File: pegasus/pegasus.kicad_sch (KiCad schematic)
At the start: 9 parts, among them IC1 Adafruit_MPL3115A2, IC2 Adafruit-BNO055-PCB, IC3 L70B-M39, IC4 RFD900, U1 Teensy4.1

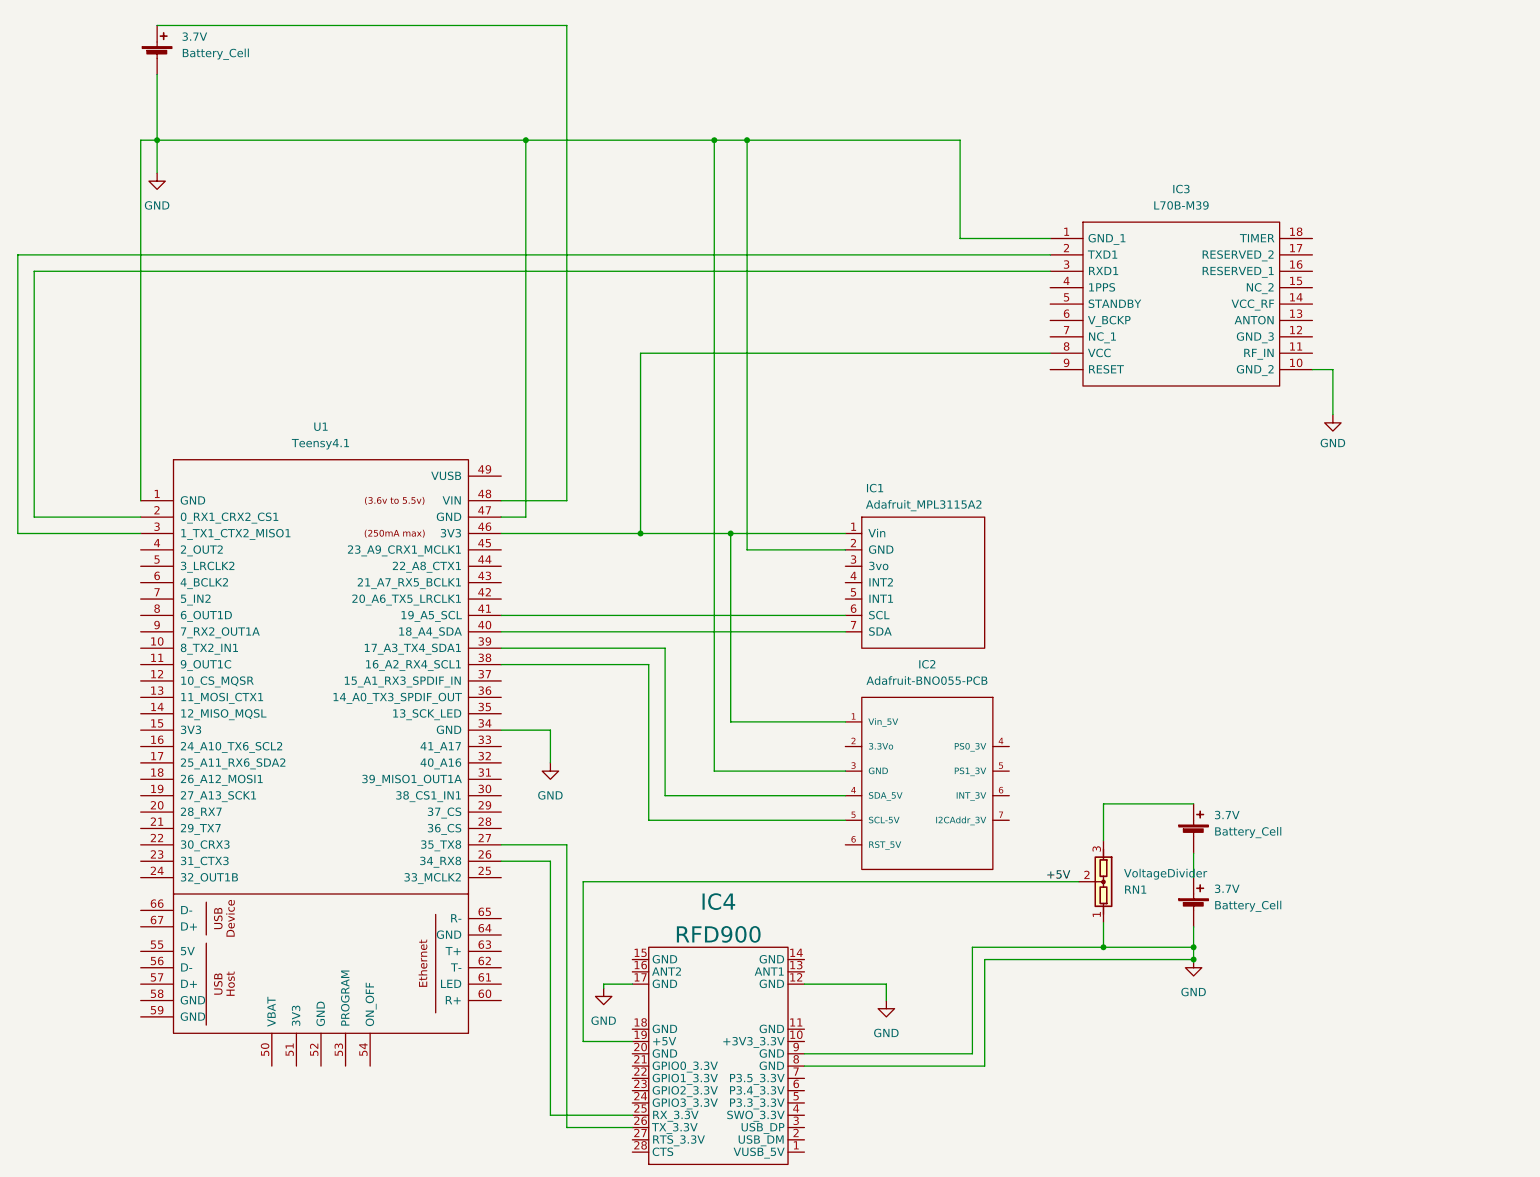
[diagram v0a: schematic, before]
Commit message: Added more components and attached footprints
added voltage regulator for rfd900, battery connectors and updated footprints for all components.
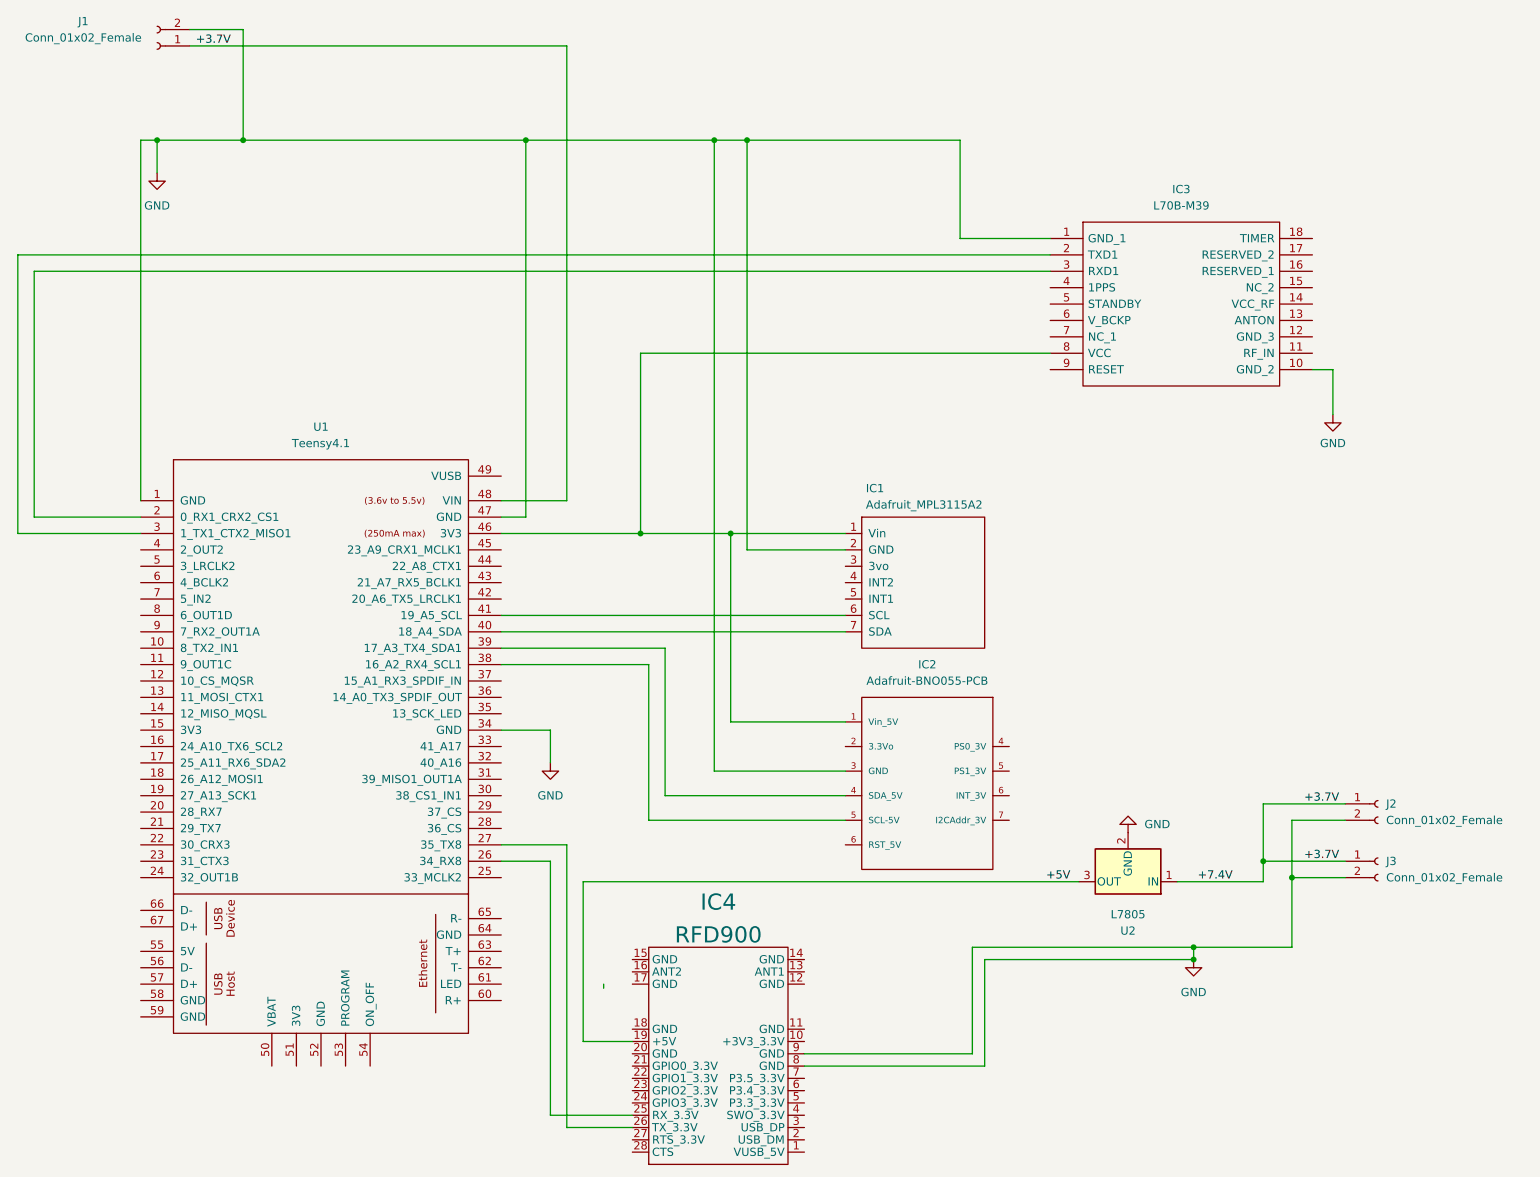
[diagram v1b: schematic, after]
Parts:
- removed 3.7V (x3): Battery_Cell, symbol Device:Battery_Cell
- removed RN1: VoltageDivider, symbol Device:VoltageDivider
- added J1, J2, J3: Conn_01x02_Female, Connector_PinHeader_2.00mm:PinHeader_1x02_P2.00mm_Horizontal, symbol Connector:Conn_01x02_Female
- added U2: L7805, symbol Regulator_Linear:L7805
- IC1: footprint MPL3115A2:1x07 -> Adafruit_MPL3115A2:1x07
- IC2: footprint BNO055:1X10_ROUND_76 -> Adafruit_BNO055:adafruit_
- U1: footprint (none) -> Teensy_4.1:Teensy_4.1
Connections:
- net +5V: now also U2.3 (OUT)
- net GND: now also J1.2 (Pin_2), J2.2 (Pin_2), J3.2 (Pin_2), U2.2 (GND); no longer IC4.12 (GND), IC4.17 (GND)
- net +3.7V: now reaches U1.48 (VIN)
- net +3.7V: now also J1.1 (Pin_1), J2.1 (Pin_1), J3.1 (Pin_1), U2.1 (IN)

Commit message: changed connector footprints from horizontal to vertical
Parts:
- J1, J2, J3: footprint Connector_PinHeader_2.00mm:PinHeader_1x02_P2.00mm_Horizontal -> Connector_PinHeader_2.00mm:PinHeader_1x02_P2.00mm_Vertical
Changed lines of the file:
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@@
       (effects (font (size 1.27 1.27)) (justify left))
     )
-    (property "Footprint" "Connector_PinHeader_2.00mm:PinHeader_1x02_P2.00mm_Horizontal" (id 2) (at 233.68 138.43 0)
+    (property "Footprint" "Connector_PinHeader_2.00mm:PinHeader_1x02_P2.00mm_Vertical" (id 2) (at 233.68 138.43 0)
       (effects (font (size 1.27 1.27)) hide)
     )
@@
       (effects (font (size 1.27 1.27)) (justify left))
     )
-    (property "Footprint" "Connector_PinHeader_2.00mm:PinHeader_1x02_P2.00mm_Horizontal" (id 2) (at 233.68 147.32 0)
+    (property "Footprint" "Connector_PinHeader_2.00mm:PinHeader_1x02_P2.00mm_Vertical" (id 2) (at 233.68 147.32 0)
       (effects (font (size 1.27 1.27)) hide)
     )
@@
     (property "Reference" "J1" (id 0) (at 33.02 17.145 0))
     (property "Value" "Conn_01x02_Female" (id 1) (at 33.02 19.685 0))
-    (property "Footprint" "Connector_PinHeader_2.00mm:PinHeader_1x02_P2.00mm_Horizontal" (id 2) (at 44.45 20.955 0)
+    (property "Footprint" "Connector_PinHeader_2.00mm:PinHeader_1x02_P2.00mm_Vertical" (id 2) (at 44.45 20.955 0)
       (effects (font (size 1.27 1.27)) hide)
     )
@@
     )
     (path "/50f78511-b951-4dcf-a410-ebb84e2ce437"
-      (reference "J1") (unit 1) (value "Conn_01x02_Female") (footprint "Connector_PinHeader_2.00mm:PinHeader_1x02_P2.00mm_Horizontal")
+      (reference "J1") (unit 1) (value "Conn_01x02_Female") (footprint "Connector_PinHeader_2.00mm:PinHeader_1x02_P2.00mm_Vertical")
     )
     (path "/0ea184c9-73d1-4b8a-8896-3886b45cbf01"
-      (reference "J2") (unit 1) (value "Conn_01x02_Female") (footprint "Connector_PinHeader_2.00mm:PinHeader_1x02_P2.00mm_Horizontal")
+      (reference "J2") (unit 1) (value "Conn_01x02_Female") (footprint "Connector_PinHeader_2.00mm:PinHeader_1x02_P2.00mm_Vertical")
     )
     (path "/419715bf-ffaa-4f14-ba39-b7cca3633324"
-      (reference "J3") (unit 1) (value "Conn_01x02_Female") (footprint "Connector_PinHeader_2.00mm:PinHeader_1x02_P2.00mm_Horizontal")
+      (reference "J3") (unit 1) (value "Conn_01x02_Female") (footprint "Connector_PinHeader_2.00mm:PinHeader_1x02_P2.00mm_Vertical")
     )
     (path "/0c9ca546-3290-4390-b47a-32e3591868b6"

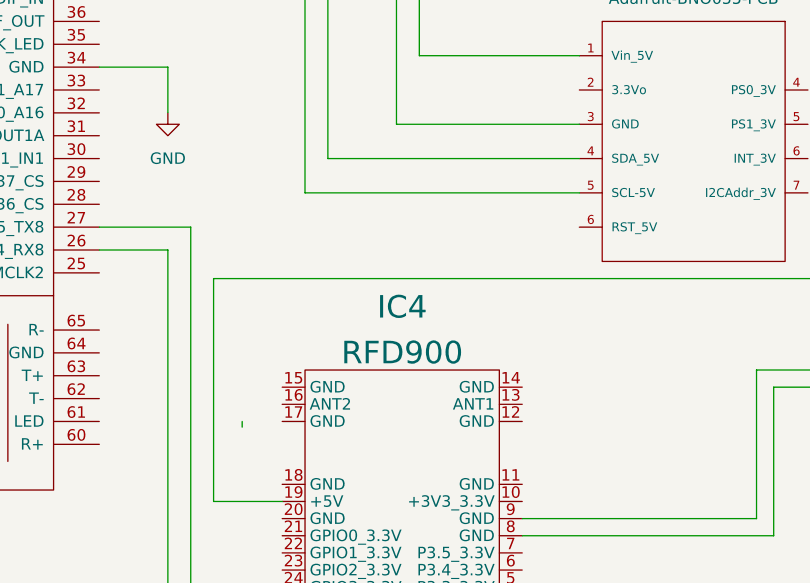
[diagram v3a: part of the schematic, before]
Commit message: adding sma coaxial connectors, footprint may change
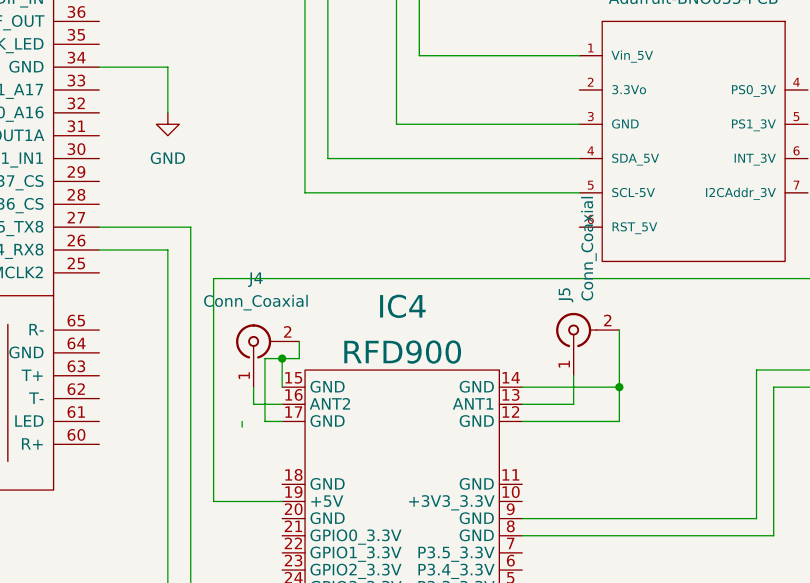
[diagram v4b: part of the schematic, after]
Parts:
- added J4, J5: Conn_Coaxial, Connector_Coaxial:SMA_Molex_73251-1153_EdgeMount_Horizontal, symbol Connector:Conn_Coaxial
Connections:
- net at IC4.12 (GND): now also IC4.14 (GND), J5.2 (Ext)
- net at IC4.13 (ANT1): now also J5.1 (In)
- net at IC4.15 (GND): now also IC4.17 (GND), J4.2 (Ext)
- net at IC4.16 (ANT2): now also J4.1 (In)
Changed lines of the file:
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@@
   (junction (at 135.89 35.56) (diameter 0) (color 0 0 0 0)
   )
+  (junction (at 118.11 159.385) (diameter 0) (color 0 0 0 0)
+  )
+  (junction (at 155.575 162.56) (diameter 0) (color 0 0 0 0)
+  )
   (junction (at 130.81 35.56) (diameter 0) (color 0 0 0 0)
   )
@@
     (stroke (width 0) (type default) (color 0 0 0 0))
   )
+  (wire (pts (xy 144.78 164.465) (xy 150.495 164.465))
+    (stroke (width 0) (type default) (color 0 0 0 0))
+  )
   (wire (pts (xy 220.345 149.86) (xy 228.6 149.86))
     (stroke (width 0) (type default) (color 0 0 0 0))
@@
     (stroke (width 0) (type default) (color 0 0 0 0))
   )
+  (wire (pts (xy 150.495 164.465) (xy 150.495 161.29))
+    (stroke (width 0) (type default) (color 0 0 0 0))
+  )
   (wire (pts (xy 133.35 125.73) (xy 151.13 125.73))
     (stroke (width 0) (type default) (color 0 0 0 0))
@@
     (stroke (width 0) (type default) (color 0 0 0 0))
   )
+  (wire (pts (xy 120.015 157.48) (xy 120.015 159.385))
+    (stroke (width 0) (type default) (color 0 0 0 0))
+  )
+  (wire (pts (xy 118.11 166.37) (xy 116.205 166.37))
+    (stroke (width 0) (type default) (color 0 0 0 0))
+  )
   (wire (pts (xy 144.78 179.07) (xy 172.72 179.07))
     (stroke (width 0) (type default) (color 0 0 0 0))
   )
+  (wire (pts (xy 116.205 159.385) (xy 118.11 159.385))
+    (stroke (width 0) (type default) (color 0 0 0 0))
+  )
   (wire (pts (xy 110.49 175.26) (xy 118.11 175.26))
     (stroke (width 0) (type default) (color 0 0 0 0))
@@
     (stroke (width 0) (type default) (color 0 0 0 0))
   )
+  (wire (pts (xy 144.78 162.56) (xy 155.575 162.56))
+    (stroke (width 0) (type default) (color 0 0 0 0))
+  )
   (wire (pts (xy 25.4 55.88) (xy 182.88 55.88))
     (stroke (width 0) (type default) (color 0 0 0 0))
@@
     (stroke (width 0) (type default) (color 0 0 0 0))
   )
+  (wire (pts (xy 155.575 162.56) (xy 155.575 166.37))
+    (stroke (width 0) (type default) (color 0 0 0 0))
+  )
   (wire (pts (xy 97.79 111.76) (xy 151.13 111.76))
     (stroke (width 0) (type default) (color 0 0 0 0))
@@
     (stroke (width 0) (type default) (color 0 0 0 0))
   )
+  (wire (pts (xy 114.935 162.56) (xy 114.935 164.465))
+    (stroke (width 0) (type default) (color 0 0 0 0))
+  )
   (wire (pts (xy 120.65 140.97) (xy 151.13 140.97))
     (stroke (width 0) (type default) (color 0 0 0 0))
@@
     (stroke (width 0) (type default) (color 0 0 0 0))
   )
+  (wire (pts (xy 118.11 159.385) (xy 118.11 162.56))
+    (stroke (width 0) (type default) (color 0 0 0 0))
+  )
   (wire (pts (xy 49.53 20.955) (xy 107.95 20.955))
     (stroke (width 0) (type default) (color 0 0 0 0))
@@
     (stroke (width 0) (type default) (color 0 0 0 0))
   )
+  (wire (pts (xy 120.015 159.385) (xy 118.11 159.385))
+    (stroke (width 0) (type default) (color 0 0 0 0))
+  )
   (wire (pts (xy 135.89 99.06) (xy 151.13 99.06))
     (stroke (width 0) (type default) (color 0 0 0 0))
@@
     (stroke (width 0) (type default) (color 0 0 0 0))
   )
+  (wire (pts (xy 155.575 162.56) (xy 155.575 156.21))
+    (stroke (width 0) (type default) (color 0 0 0 0))
+  )
   (wire (pts (xy 202.565 150.495) (xy 215.9 150.495))
     (stroke (width 0) (type default) (color 0 0 0 0))
@@
     (stroke (width 0) (type default) (color 0 0 0 0))
   )
+  (wire (pts (xy 155.575 166.37) (xy 144.78 166.37))
+    (stroke (width 0) (type default) (color 0 0 0 0))
+  )
   (wire (pts (xy 119.38 68.58) (xy 119.38 96.52))
     (stroke (width 0) (type default) (color 0 0 0 0))
@@
     (stroke (width 0) (type default) (color 0 0 0 0))
   )
+  (wire (pts (xy 116.205 166.37) (xy 116.205 159.385))
+    (stroke (width 0) (type default) (color 0 0 0 0))
+  )
   (wire (pts (xy 41.91 35.56) (xy 44.45 35.56))
+    (stroke (width 0) (type default) (color 0 0 0 0))
+  )
+  (wire (pts (xy 114.935 164.465) (xy 118.11 164.465))
     (stroke (width 0) (type default) (color 0 0 0 0))
   )
@@
     (pin "1")
   )
+  (symbol (lib_id "Connector:Conn_Coaxial") (at 114.935 157.48 90) (unit 1)
+    (in_bom yes) (on_board yes) (fields_autoplaced)
+    (property "Reference" "J4" (id 0) (at 115.2282 150.495 90))
+    (property "Value" "Conn_Coaxial" (id 1) (at 115.2282 153.035 90))
+    (property "Footprint" "Connector_Coaxial:SMA_Molex_73251-1153_EdgeMount_Horizontal" (id 2) (at 114.935 157.48 0)
+      (effects (font (size 1.27 1.27)) hide)
+    )
+    (property "Datasheet" " ~" (id 3) (at 114.935 157.48 0)
+      (effects (font (size 1.27 1.27)) hide)
+    )
+    (pin "1")
+    (pin "2")
+  )
   (symbol (lib_id "Connector:Conn_01x02_Female") (at 233.68 147.32 0) (unit 1)
     (in_bom yes) (on_board yes) (fields_autoplaced)
@@
     (pin "8")
     (pin "9")
+  )
+  (symbol (lib_id "Connector:Conn_Coaxial") (at 150.495 156.21 90) (unit 1)
+    (in_bom yes) (on_board yes) (fields_autoplaced)
+    (property "Reference" "J5" (id 0) (at 149.5181 153.035 0)
+      (effects (font (size 1.27 1.27)) (justify left))
+    )
+    (property "Value" "Conn_Coaxial" (id 1) (at 152.0581 153.035 0)
+      (effects (font (size 1.27 1.27)) (justify left))
+    )
+    (property "Footprint" "Connector_Coaxial:SMA_Molex_73251-1153_EdgeMount_Horizontal" (id 2) (at 150.495 156.21 0)
+      (effects (font (size 1.27 1.27)) hide)
+    )
+    (property "Datasheet" " ~" (id 3) (at 150.495 156.21 0)
+      (effects (font (size 1.27 1.27)) hide)
+    )
+    (pin "1")
+    (pin "2")
   )
   (symbol (lib_id "Adafruit_BNO055:Adafruit-BNO055-PCB") (at 164.465 140.335 180) (unit 1)
@@
       (reference "J3") (unit 1) (value "Conn_01x02_Female") (footprint "Connector_PinHeader_2.00mm:PinHeader_1x02_P2.00mm_Vertical")
     )
+    (path "/3ccf6afc-bd28-4aa2-895e-eba52cf09e27"
+      (reference "J4") (unit 1) (value "Conn_Coaxial") (footprint "Connector_Coaxial:SMA_Molex_73251-1153_EdgeMount_Horizontal")
+    )
+    (path "/c03f4d5e-77ae-49b9-9ca6-c3a4322933e2"
+      (reference "J5") (unit 1) (value "Conn_Coaxial") (footprint "Connector_Coaxial:SMA_Molex_73251-1153_EdgeMount_Horizontal")
+    )
     (path "/0c9ca546-3290-4390-b47a-32e3591868b6"
